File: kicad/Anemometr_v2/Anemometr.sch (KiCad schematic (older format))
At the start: 157 parts, among them J1 TxD, J10 +Z1, J11 +Z2, J12 +Z3, J13 +Z4, J14 -Z1, J15 -Z2, J16 -Z3, J17 -Z4, J18 1 TxD+, J19 2 TxD-, J2 RxD, J20 3 RxD+, J21 4-5, J22 6 RxD-, J23 7-8, J24 Conn_01x01_Female, J25 Conn_01x01_Female, J3 SCL, J4 SDA, J5 RST, J6 +EXT, J7 -EXT, J8 SWD, J9 SWC, Q1 5N10, U1 STM32F103C8Tx, U2 TS5A3166DBVR, U3 TS5A3166DBVR, U4 TS5A3166DBVR, U5 TS5A3166DBVR, U6 NCP1117-3.3, U7 MCP1703-5, U8 TLV3201DBV, U9 MCP1703-3.3, Y1 CSTCE8M00G52A-R0, Y2 ECS-250-20-33

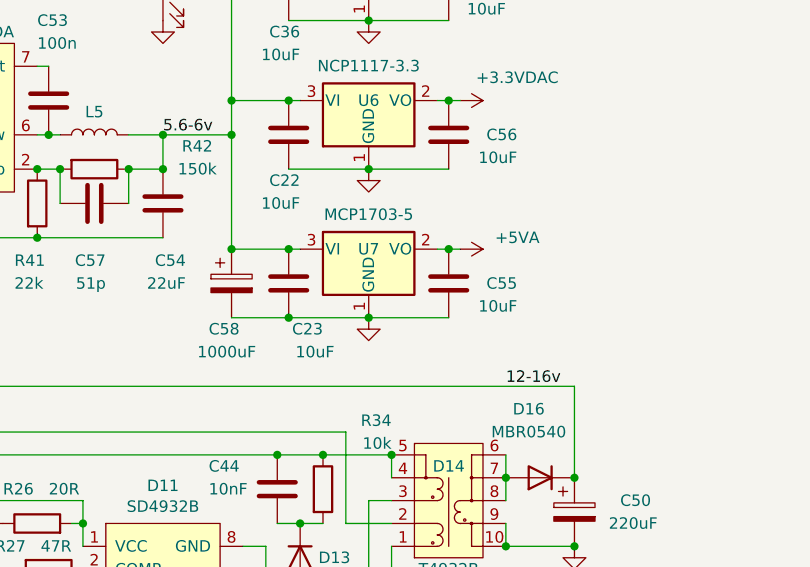
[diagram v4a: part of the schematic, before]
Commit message: изменено:      FreeCAD/holder-3.fcstd 	изменено:      kicad/Anemometr_v2/Anemometr.kicad_pcb 	изменено:      kicad/Anemometr_v2/Anemometr.kicad_pcb-bak 	изменено:      kicad/Anemometr_v2/Anemometr.sch 	изменено:      kicad/Anemometr_v2/Anemometr.sch-bak 	изменено:      kicad/Anemometr_v2/fp-info-cache
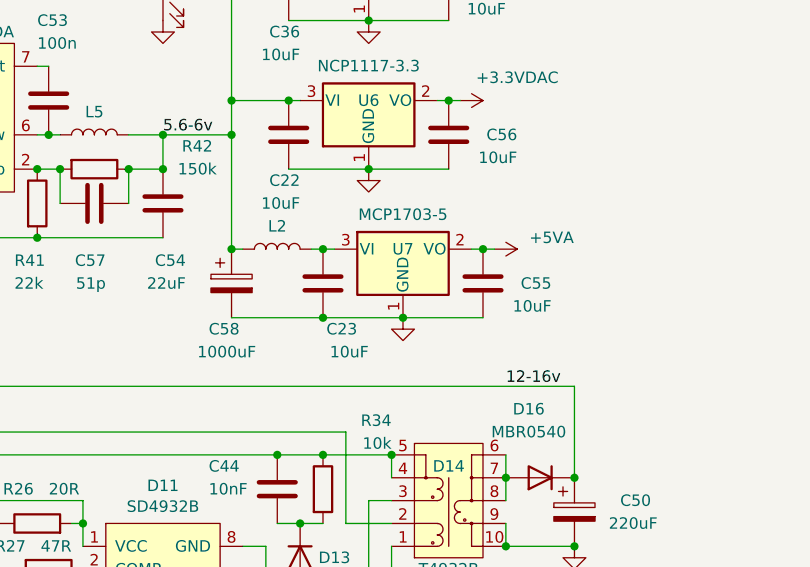
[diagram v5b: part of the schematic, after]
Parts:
- added L2: 47uH, Inductor_SMD:L_0805_2012Metric, symbol Device:L
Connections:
- net 5.6-6v: now also L2.1; no longer C23.2, U7.3 (VI)
- new net: C23.2, L2.2, U7.3 (VI)
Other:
- moved on the sheet: C23, C55, U7
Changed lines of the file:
@@
 L Device:C C23
 U 1 1 61DF7EFE
-P 10400 4450
-F 0 "C23" H 10250 4650 50  0000 L CNN
-F 1 "10uF" H 10200 4750 50  0000 L CNN
-F 2 "Capacitor_SMD:C_0805_2012Metric" H 10438 4300 50  0001 C CNN
-F 3 "~" H 10400 4450 50  0001 C CNN
-	1    10400 4450
+P 10550 4450
+F 0 "C23" H 10400 4650 50  0000 L CNN
+F 1 "10uF" H 10350 4750 50  0000 L CNN
+F 2 "Capacitor_SMD:C_0805_2012Metric" H 10588 4300 50  0001 C CNN
+F 3 "~" H 10550 4450 50  0001 C CNN
+	1    10550 4450
 	-1   0    0    1
 $EndComp
@@
 L power:+5VA #PWR061
 U 1 1 61E509BB
-P 11150 4300
-F 0 "#PWR061" H 11150 4150 50  0001 C CNN
-F 1 "+5VA" V 11100 4550 50  0000 C CNN
-F 2 "" H 11150 4300 50  0001 C CNN
-F 3 "" H 11150 4300 50  0001 C CNN
-	1    11150 4300
+P 11300 4300
+F 0 "#PWR061" H 11300 4150 50  0001 C CNN
+F 1 "+5VA" V 11250 4550 50  0000 C CNN
+F 2 "" H 11300 4300 50  0001 C CNN
+F 3 "" H 11300 4300 50  0001 C CNN
+	1    11300 4300
 	0    1    1    0
 $EndComp
@@
 L power:GND #PWR060
 U 1 1 62428E08
-P 10750 4600
-F 0 "#PWR060" H 10750 4350 50  0001 C CNN
-F 1 "GND" H 10755 4427 50  0001 C CNN
-F 2 "" H 10750 4600 50  0001 C CNN
-F 3 "" H 10750 4600 50  0001 C CNN
-	1    10750 4600
+P 10900 4600
+F 0 "#PWR060" H 10900 4350 50  0001 C CNN
+F 1 "GND" H 10905 4427 50  0001 C CNN
+F 2 "" H 10900 4600 50  0001 C CNN
+F 3 "" H 10900 4600 50  0001 C CNN
+	1    10900 4600
 	1    0    0    -1
 $EndComp
@@
 L Device:C C55
 U 1 1 62B0B8C5
-P 11100 4450
-F 0 "C55" H 10800 4450 50  0000 L CNN
-F 1 "10uF" H 10800 4550 50  0000 L CNN
-F 2 "Capacitor_SMD:C_0805_2012Metric" H 11138 4300 50  0001 C CNN
-F 3 "~" H 11100 4450 50  0001 C CNN
-	1    11100 4450
+P 11250 4450
+F 0 "C55" H 10950 4450 50  0000 L CNN
+F 1 "10uF" H 10950 4550 50  0000 L CNN
+F 2 "Capacitor_SMD:C_0805_2012Metric" H 11288 4300 50  0001 C CNN
+F 3 "~" H 11250 4450 50  0001 C CNN
+	1    11250 4450
 	-1   0    0    1
 $EndComp
@@
 L Regulator_Linear:MCP1700-5002E_SOT23 U7
 U 1 1 62D8FA20
-P 10750 4300
-F 0 "U7" H 10750 4300 50  0000 C CNN
-F 1 "MCP1703-5" H 10750 4451 50  0000 C CNN
-F 2 "Package_TO_SOT_SMD:SOT-23" H 10750 4525 50  0001 C CNN
-F 3 "http://ww1.microchip.com/downloads/en/DeviceDoc/20001826C.pdf" H 10750 4300 50  0001 C CNN
-	1    10750 4300
+P 10900 4300
+F 0 "U7" H 10900 4300 50  0000 C CNN
+F 1 "MCP1703-5" H 10900 4451 50  0000 C CNN
+F 2 "Package_TO_SOT_SMD:SOT-23" H 10900 4525 50  0001 C CNN
+F 3 "http://ww1.microchip.com/downloads/en/DeviceDoc/20001826C.pdf" H 10900 4300 50  0001 C CNN
+	1    10900 4300
 	1    0    0    -1
 $EndComp
@@
 	10750 3950 11100 3950
 Wire Wire Line
-	10400 4600 10750 4600
-Connection ~ 10750 4600
-Wire Wire Line
-	10750 4600 11100 4600
-Wire Wire Line
-	11050 4300 11100 4300
-Connection ~ 11100 4300
-Wire Wire Line
-	11100 4300 11150 4300
-Wire Wire Line
-	10400 4300 10450 4300
+	10550 4600 10900 4600
+Connection ~ 10900 4600
+Wire Wire Line
+	10900 4600 11250 4600
+Wire Wire Line
+	11200 4300 11250 4300
+Connection ~ 11250 4300
+Wire Wire Line
+	11250 4300 11300 4300
+Wire Wire Line
+	10550 4300 10600 4300
 Connection ~ 10400 3650
 Wire Wire Line
@@
 	10450 3000 10400 3000
 Connection ~ 10400 3000
-Connection ~ 10400 4300
 Connection ~ 8550 4250
 Wire Wire Line
@@
 	1    0    0    -1
 $EndComp
-Connection ~ 10400 4600
-Wire Wire Line
-	10150 4600 10400 4600
 Wire Wire Line
 	10150 4300 10150 3800
@@
 Wire Wire Line
 	10150 3800 10150 3650
-Wire Wire Line
-	10150 4300 10400 4300
-Connection ~ 10150 4300
 Wire Wire Line
 	6350 5050 6800 5050
@@
 Analog
 NoConn ~ 5750 4350
+$Comp
+L Device:L L2
+U 1 1 62A3E097
+P 10350 4300
+F 0 "L2" V 10450 4300 50  0000 C CNN
+F 1 "47uH" V 10450 4250 50  0001 C CNN
+F 2 "Inductor_SMD:L_0805_2012Metric" H 10350 4300 50  0001 C CNN
+F 3 "~" H 10350 4300 50  0001 C CNN
+	1    10350 4300
+	0    -1   -1   0
+$EndComp
+Wire Wire Line
+	10200 4300 10150 4300
+Connection ~ 10150 4300
+Wire Wire Line
+	10500 4300 10550 4300
+Connection ~ 10550 4300
+Wire Wire Line
+	10150 4600 10550 4600
+Connection ~ 10550 4600
 $EndSCHEMATC
